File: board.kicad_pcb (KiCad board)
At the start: 2 copper layers, 49 parts, among them J1 TEMPS, J2 OLED, J3 Screw_Terminal_01x03, J4 Screw_Terminal_01x03, J5 PWR_IN, J6 CONN_PROG, J6 Conn_01x05_Female, K2 SRD-05VDC-SL-C, K3 SRD-05VDC-SL-C, Q1 BC847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

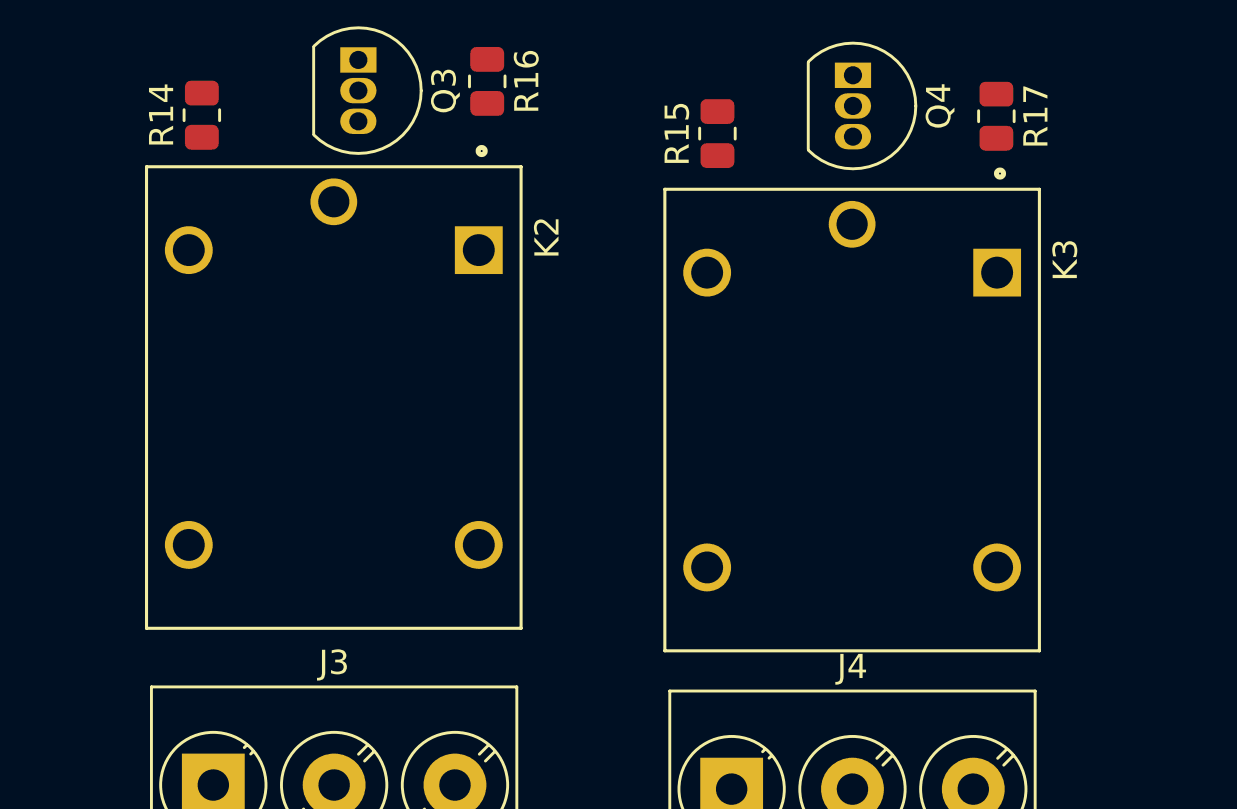
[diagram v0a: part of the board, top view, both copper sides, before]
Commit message: feat: added relative pathing for relay libs
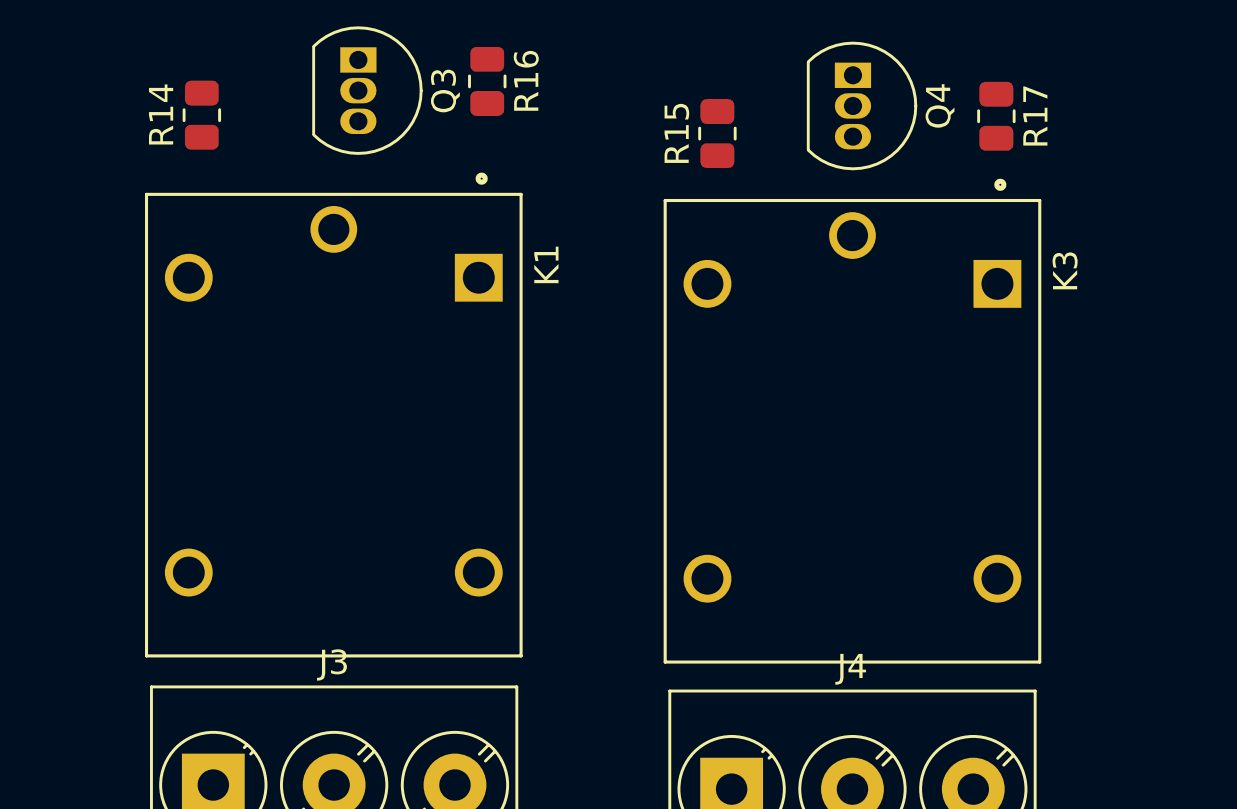
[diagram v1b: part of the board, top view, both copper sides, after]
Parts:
- removed K2: SRD-05VDC-SL-C, SRD-05VDC-SL-C:RELAY_SRD-05VDC-SL-C
- added K1: SRD-05VDC-SL-C, SRD-05VDC-SL-C:RELAY_SRD-05VDC-SL-C, F.Cu at (54.7, 97.4)
- moved K3 0.47 mm to (76.2, 97.7)
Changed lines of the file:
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@@
   (net 67 "Net-(J3-Pad1)")
   (net 68 "Net-(J3-Pad3)")
-  (net 69 "Net-(R17-Pad2)")
+  (net 69 "Net-(K3-PadA1)")
   (net 70 "Net-(J4-Pad2)")
   (net 71 "Net-(J4-Pad1)")
@@
       (net 64 "Net-(Q4-Pad1)") (pintype "passive"))
     (pad "2" smd roundrect (at 0.9125 0 270) (size 1.025 1.4) (layers "F.Cu" "F.Paste" "F.Mask") (roundrect_rratio 0.243902)
-      (net 69 "Net-(R17-Pad2)") (pintype "passive"))
+      (net 69 "Net-(K3-PadA1)") (pintype "passive"))
     (model "${KICAD6_3DMODEL_DIR}/Resistor_SMD.3dshapes/R_0805_2012Metric.wrl"
       (offset (xyz 0 0 0))
@@
     )
   )
+  (footprint "SRD-05VDC-SL-C:RELAY_SRD-05VDC-SL-C" (layer "F.Cu")
+    (at 54.737 97.409 -90)
+    (property "MANUFACTURER" "SONGLE RELAY")
+    (property "STANDARD" "IPC-7251")
+    (property "Sheetfile" "board.kicad_sch")
+    (property "Sheetname" "")
+    (attr through_hole)
+    (fp_text reference "K1" (at -6.62563 -8.83584 90) (layer "F.SilkS")
+      (effects (font (size 1.000094 1.000094) (thickness 0.15)))
+    )
+    (fp_text value "SRD-05VDC-SL-C" (at 2.90086 8.667695 90) (layer "F.Fab")
+      (effects (font (size 1.000307 1.000307) (thickness 0.15)))
+    )
+    (fp_line (start 9.55 7.75) (end -9.55 7.75) (layer "F.SilkS") (width 0.127))
+    (fp_line (start -9.55 7.75) (end -9.55 -7.75) (layer "F.SilkS") (width 0.127))
+    (fp_line (start -9.55 -7.75) (end 9.55 -7.75) (layer "F.SilkS") (width 0.127))
+    (fp_line (start 9.55 -7.75) (end 9.55 7.75) (layer "F.SilkS") (width 0.127))
+    (fp_circle (center -10.2 -6.119) (end -10.1 -6.119) (layer "F.SilkS") (width 0.3) (fill none))
+    (fp_line (start 9.8 -8) (end 9.8 8) (layer "F.CrtYd") (width 0.05))
+    (fp_line (start 9.8 8) (end -9.8 8) (layer "F.CrtYd") (width 0.05))
+    (fp_line (start -9.8 8) (end -9.8 -8) (layer "F.CrtYd") (width 0.05))
+    (fp_line (start -9.8 -8) (end 9.8 -8) (layer "F.CrtYd") (width 0.05))
+    (fp_line (start 9.55 -7.75) (end 9.55 7.75) (layer "F.Fab") (width 0.127))
+    (fp_line (start 9.55 7.75) (end -9.55 7.75) (layer "F.Fab") (width 0.127))
+    (fp_line (start -9.55 7.75) (end -9.55 -7.75) (layer "F.Fab") (width 0.127))
+    (fp_line (start -9.55 -7.75) (end 9.55 -7.75) (layer "F.Fab") (width 0.127))
+    (pad "A1" thru_hole rect (at -6.1 -6 270) (size 1.98 1.98) (drill 1.32) (layers *.Cu *.Mask)
+      (net 65 "Net-(R16-Pad2)") (pintype "passive"))
+    (pad "A2" thru_hole circle (at -6.1 6 270) (size 1.98 1.98) (drill 1.32) (layers *.Cu *.Mask)
+      (net 3 "VBUS") (pintype "passive"))
+    (pad "COM" thru_hole circle (at -8.1 0 270) (size 1.935 1.935) (drill 1.29) (layers *.Cu *.Mask)
+      (net 66 "Net-(J3-Pad2)") (pintype "passive"))
+    (pad "NC" thru_hole circle (at 6.1 -6 270) (size 1.98 1.98) (drill 1.32) (layers *.Cu *.Mask)
+      (net 68 "Net-(J3-Pad3)") (pintype "passive"))
+    (pad "NO" thru_hole circle (at 6.1 6 270) (size 1.98 1.98) (drill 1.32) (layers *.Cu *.Mask)
+      (net 67 "Net-(J3-Pad1)") (pintype "passive"))
+    (model "${KIPRJMOD}/libs/SRD-05VDC-SL-C/SRD-05VDC-SL-C.step"
+      (offset (xyz 9 7.5 0))
+      (scale (xyz 1 1 1))
+      (rotate (xyz 0 0 180))
+    )
+  )
   (footprint "Resistor_SMD:R_0805_2012Metric" (layer "F.Cu")
     (at 49.8035 52.514 180)
@@
   )
   (footprint "SRD-05VDC-SL-C:RELAY_SRD-05VDC-SL-C" (layer "F.Cu")
-    (at 54.737 96.266 -90)
+    (at 76.2 97.663 -90)
     (property "MANUFACTURER" "SONGLE RELAY")
     (property "STANDARD" "IPC-7251")
@@
     (property "Sheetname" "")
     (attr through_hole)
-    (fp_text reference "K2" (at -6.62563 -8.83584 90) (layer "F.SilkS")
+    (fp_text reference "K3" (at -6.62563 -8.83584 90) (layer "F.SilkS")
       (effects (font (size 1.000094 1.000094) (thickness 0.15)))
     )
@@
       (effects (font (size 1.000307 1.000307) (thickness 0.15)))
     )
-    (fp_line (start -9.55 -7.75) (end 9.55 -7.75) (layer "F.SilkS") (width 0.127))
     (fp_line (start 9.55 -7.75) (end 9.55 7.75) (layer "F.SilkS") (width 0.127))
     (fp_line (start -9.55 7.75) (end -9.55 -7.75) (layer "F.SilkS") (width 0.127))
+    (fp_line (start -9.55 -7.75) (end 9.55 -7.75) (layer "F.SilkS") (width 0.127))
     (fp_line (start 9.55 7.75) (end -9.55 7.75) (layer "F.SilkS") (width 0.127))
     (fp_circle (center -10.2 -6.119) (end -10.1 -6.119) (layer "F.SilkS") (width 0.3) (fill none))
+    (fp_line (start -9.8 -8) (end 9.8 -8) (layer "F.CrtYd") (width 0.05))
+    (fp_line (start 9.8 -8) (end 9.8 8) (layer "F.CrtYd") (width 0.05))
+    (fp_line (start 9.8 8) (end -9.8 8) (layer "F.CrtYd") (width 0.05))
     (fp_line (start -9.8 8) (end -9.8 -8) (layer "F.CrtYd") (width 0.05))
-    (fp_line (start 9.8 -8) (end 9.8 8) (layer "F.CrtYd") (width 0.05))
-    (fp_line (start -9.8 -8) (end 9.8 -8) (layer "F.CrtYd") (width 0.05))
-    (fp_line (start 9.8 8) (end -9.8 8) (layer "F.CrtYd") (width 0.05))
+    (fp_line (start 9.55 7.75) (end -9.55 7.75) (layer "F.Fab") (width 0.127))
+    (fp_line (start 9.55 -7.75) (end 9.55 7.75) (layer "F.Fab") (width 0.127))
     (fp_line (start -9.55 -7.75) (end 9.55 -7.75) (layer "F.Fab") (width 0.127))
-    (fp_line (start 9.55 -7.75) (end 9.55 7.75) (layer "F.Fab") (width 0.127))
-    (fp_line (start 9.55 7.75) (end -9.55 7.75) (layer "F.Fab") (width 0.127))
     (fp_line (start -9.55 7.75) (end -9.55 -7.75) (layer "F.Fab") (width 0.127))
-    (pad "A1" thru_hole rect locked (at -6.1 -6 270) (size 1.98 1.98) (drill 1.32) (layers *.Cu *.Mask)
-      (net 65 "Net-(R16-Pad2)") (pintype "passive"))
-    (pad "A2" thru_hole circle locked (at -6.1 6 270) (size 1.98 1.98) (drill 1.32) (layers *.Cu *.Mask)
+    (pad "A1" thru_hole rect (at -6.1 -6 270) (size 1.98 1.98) (drill 1.32) (layers *.Cu *.Mask)
+      (net 69 "Net-(K3-PadA1)") (pintype "passive"))
+    (pad "A2" thru_hole circle (at -6.1 6 270) (size 1.98 1.98) (drill 1.32) (layers *.Cu *.Mask)
       (net 3 "VBUS") (pintype "passive"))
-    (pad "COM" thru_hole circle locked (at -8.1 0 270) (size 1.935 1.935) (drill 1.29) (layers *.Cu *.Mask)
-      (net 66 "Net-(J3-Pad2)") (pintype "passive"))
-    (pad "NC" thru_hole circle locked (at 6.1 -6 270) (size 1.98 1.98) (drill 1.32) (layers *.Cu *.Mask)
-      (net 68 "Net-(J3-Pad3)") (pintype "passive"))
-    (pad "NO" thru_hole circle locked (at 6.1 6 270) (size 1.98 1.98) (drill 1.32) (layers *.Cu *.Mask)
-      (net 67 "Net-(J3-Pad1)") (pintype "passive"))
+    (pad "COM" thru_hole circle (at -8.1 0 270) (size 1.935 1.935) (drill 1.29) (layers *.Cu *.Mask)
+      (net 70 "Net-(J4-Pad2)") (pintype "passive"))
+    (pad "NC" thru_hole circle (at 6.1 -6 270) (size 1.98 1.98) (drill 1.32) (layers *.Cu *.Mask)
+      (net 72 "Net-(J4-Pad3)") (pintype "passive"))
+    (pad "NO" thru_hole circle (at 6.1 6 270) (size 1.98 1.98) (drill 1.32) (layers *.Cu *.Mask)
+      (net 71 "Net-(J4-Pad1)") (pintype "passive"))
+    (model "${KIPRJMOD}/libs/SRD-05VDC-SL-C/SRD-05VDC-SL-C.step"
+      (offset (xyz 9 7.5 0))
+      (scale (xyz 1 1 1))
+      (rotate (xyz 0 0 180))
+    )
   )
   (footprint "Resistor_SMD:R_0805_2012Metric" (layer "F.Cu")
@@
     )
   )
-  (footprint "SRD-05VDC-SL-C:RELAY_SRD-05VDC-SL-C" (layer "F.Cu")
-    (at 76.186 97.198 -90)
-    (property "MANUFACTURER" "SONGLE RELAY")
-    (property "STANDARD" "IPC-7251")
-    (property "Sheetfile" "board.kicad_sch")
-    (property "Sheetname" "")
-    (attr through_hole)
-    (fp_text reference "K3" (at -6.62563 -8.83584 90) (layer "F.SilkS")
-      (effects (font (size 1.000094 1.000094) (thickness 0.15)))
-    )
-    (fp_text value "SRD-05VDC-SL-C" (at 2.90086 8.667695 90) (layer "F.Fab")
-      (effects (font (size 1.000307 1.000307) (thickness 0.15)))
-    )
-    (fp_line (start 9.55 7.75) (end -9.55 7.75) (layer "F.SilkS") (width 0.127))
-    (fp_line (start -9.55 -7.75) (end 9.55 -7.75) (layer "F.SilkS") (width 0.127))
-    (fp_line (start 9.55 -7.75) (end 9.55 7.75) (layer "F.SilkS") (width 0.127))
-    (fp_line (start -9.55 7.75) (end -9.55 -7.75) (layer "F.SilkS") (width 0.127))
-    (fp_circle (center -10.2 -6.119) (end -10.1 -6.119) (layer "F.SilkS") (width 0.3) (fill none))
-    (fp_line (start -9.8 8) (end -9.8 -8) (layer "F.CrtYd") (width 0.05))
-    (fp_line (start -9.8 -8) (end 9.8 -8) (layer "F.CrtYd") (width 0.05))
-    (fp_line (start 9.8 -8) (end 9.8 8) (layer "F.CrtYd") (width 0.05))
-    (fp_line (start 9.8 8) (end -9.8 8) (layer "F.CrtYd") (width 0.05))
-    (fp_line (start 9.55 7.75) (end -9.55 7.75) (layer "F.Fab") (width 0.127))
-    (fp_line (start 9.55 -7.75) (end 9.55 7.75) (layer "F.Fab") (width 0.127))
-    (fp_line (start -9.55 7.75) (end -9.55 -7.75) (layer "F.Fab") (width 0.127))
-    (fp_line (start -9.55 -7.75) (end 9.55 -7.75) (layer "F.Fab") (width 0.127))
-    (pad "A1" thru_hole rect locked (at -6.1 -6 270) (size 1.98 1.98) (drill 1.32) (layers *.Cu *.Mask)
-      (net 69 "Net-(R17-Pad2)") (pintype "passive"))
-    (pad "A2" thru_hole circle locked (at -6.1 6 270) (size 1.98 1.98) (drill 1.32) (layers *.Cu *.Mask)
-      (net 3 "VBUS") (pintype "passive"))
-    (pad "COM" thru_hole circle locked (at -8.1 0 270) (size 1.935 1.935) (drill 1.29) (layers *.Cu *.Mask)
-      (net 70 "Net-(J4-Pad2)") (pintype "passive"))
-    (pad "NC" thru_hole circle locked (at 6.1 -6 270) (size 1.98 1.98) (drill 1.32) (layers *.Cu *.Mask)
-      (net 72 "Net-(J4-Pad3)") (pintype "passive"))
-    (pad "NO" thru_hole circle locked (at 6.1 6 270) (size 1.98 1.98) (drill 1.32) (layers *.Cu *.Mask)
-      (net 71 "Net-(J4-Pad1)") (pintype "passive"))
-  )
   (footprint "Button_Switch_THT:SW_PUSH_6mm_H13mm" (layer "F.Cu")

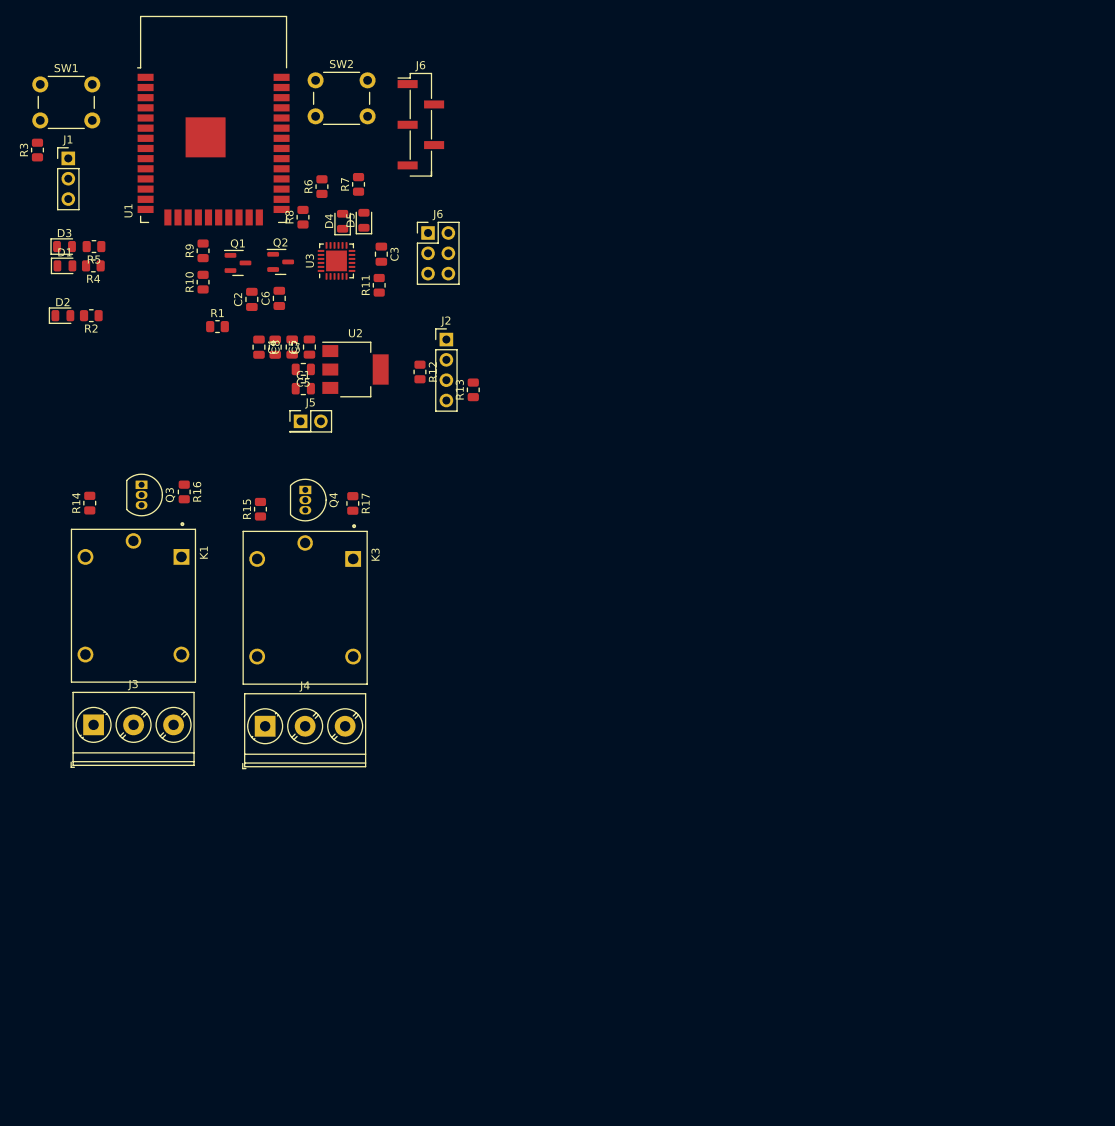
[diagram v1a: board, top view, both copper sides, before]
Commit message: feat: added usb-c connector and switched to ch340e
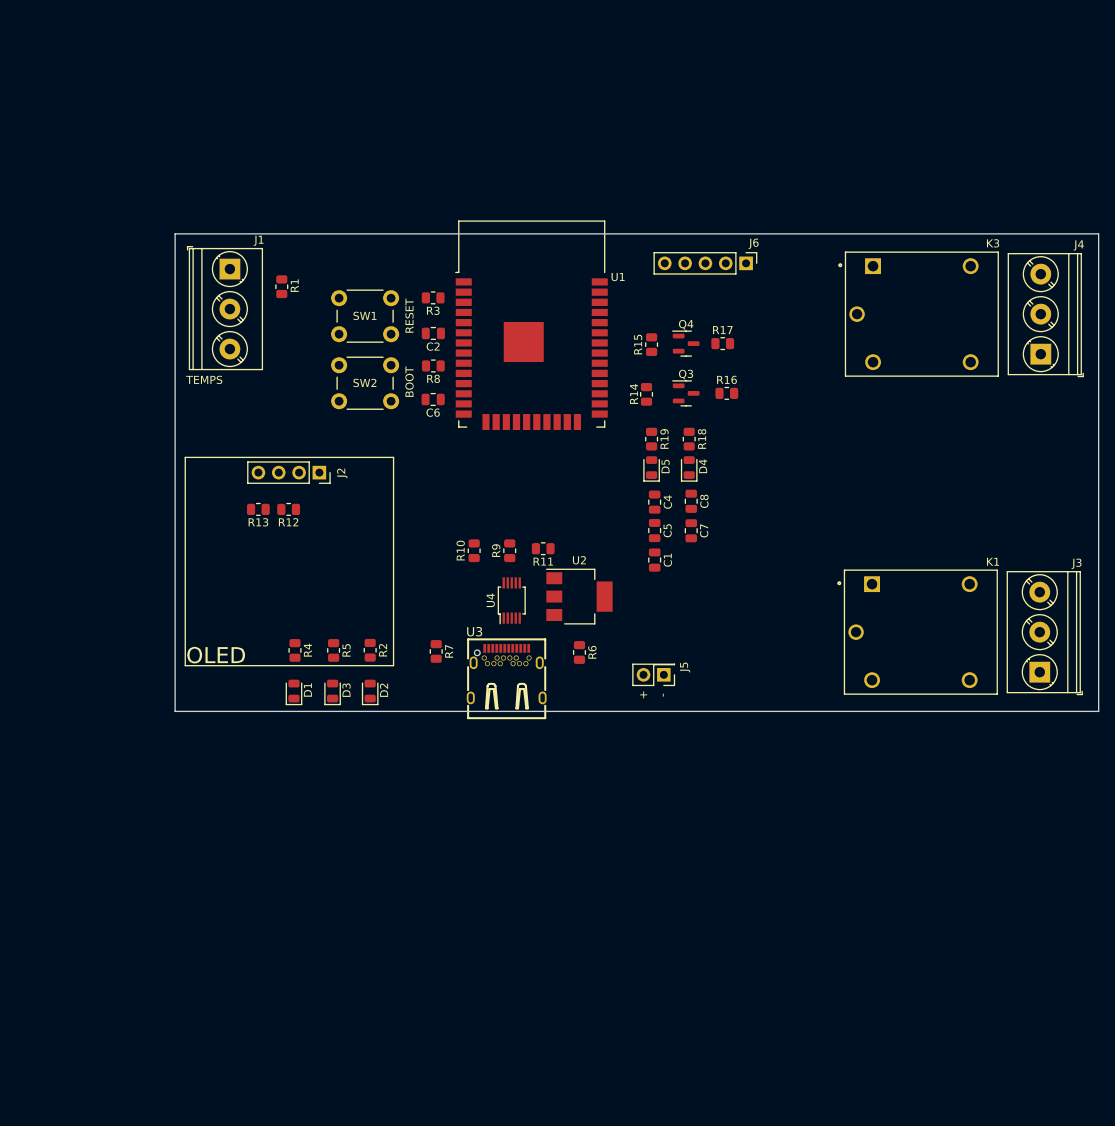
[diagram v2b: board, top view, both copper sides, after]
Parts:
- removed C3: 4.7uF, Capacitor_SMD:C_0805_2012Metric
- removed the C5 at (76.0, 67.9)
- removed the C5 at (74.6, 65.1)
- removed the J6 at (91.6, 50.8)
- removed the J6 at (90.7, 37.3)
- removed Q1, Q2: BC847, Package_TO_SOT_SMD:SOT-23
- added C5: 100nF, Capacitor_SMD:C_0805_2012Metric, F.Cu at (119.9, 88.0)
- added J6: PROG, Connector_PinHeader_2.54mm:PinHeader_1x05_P2.54mm_Vertical, F.Cu at (131.3, 54.6)
- added R18: 1k, Resistor_SMD:R_0805_2012Metric, F.Cu at (124.2, 76.6)
- added R19: 1k, Resistor_SMD:R_0805_2012Metric, F.Cu at (119.5, 76.6)
- added U4: CH340E, Package_SO:MSOP-10_3x3mm_P0.5mm, F.Cu at (102.0, 96.8)
- D4: value TXLED -> RXLED
- D5: value RXLED -> TXLED
- J1: footprint Connector_PinHeader_2.54mm:PinHeader_1x03_P2.54mm_Vertical -> TerminalBlock_Phoenix:TerminalBlock_Phoenix_PT-1,5-3-5.0-H_1x03_P5.00mm_Horizontal
- J2: footprint Connector_PinHeader_2.54mm:PinHeader_1x04_P2.54mm_Vertical -> Connector_PinSocket_2.54mm:PinSocket_1x04_P2.54mm_Vertical
- J3: value Screw_Terminal_01x03 -> HV1
- J4: value Screw_Terminal_01x03 -> HV2
- K1: value SRD-05VDC-SL-C -> RELAY1
- K3: value SRD-05VDC-SL-C -> RELAY2
- Q3, Q4: value BS170 -> AO3400A; footprint Package_TO_SOT_THT:TO-92_Inline -> Package_TO_SOT_SMD:SOT-23
- R10, R9: value 10k -> 0
- R11: value 4k7 -> 5k1
- R14, R15: value R -> 10k
- R16, R17: value R -> 0
- R6, R7: value 470 -> 5k1
- SW1: footprint Button_Switch_THT:SW_PUSH_6mm_H13mm -> Button_Switch_THT:SW_PUSH_6mm_H4.3mm
- SW2: value SW_RST -> SW_BOOT; footprint Button_Switch_THT:SW_PUSH_6mm_H13mm -> Button_Switch_THT:SW_PUSH_6mm_H4.3mm
- U1: value ESP32-WROOM-32(8MB) -> ESP32-WROOM-32
- U3: value CP2104 -> USB-306C; footprint Package_DFN_QFN:QFN-24-1EP_4x4mm_P0.5mm_EP2.6x2.6mm -> board:USB-TYPE-C-TH_USB-306C
- moved J3 118.5 mm to (168.0, 105.7), turned to 90 degrees
- moved J4 107.5 mm to (168.2, 66.0), turned to 90 degrees
- moved K1 98.5 mm to (153.2, 100.7), turned to 0 degrees
- moved K3 85.4 mm to (153.3, 61.0), turned to 0 degrees
- moved R14 70.9 mm to (118.9, 71.0)
- moved Q3 69.0 mm to (123.8, 70.9), turned to 0 degrees
- moved R16 68.9 mm to (128.9, 70.9), turned to 0 degrees
- moved R6 66.5 mm to (110.5, 103.3), turned to -90 degrees
- moved D3 64.9 mm to (79.6, 108.1), turned to 90 degrees
- moved D2 60.6 mm to (84.3, 108.1), turned to 90 degrees
- moved D1 60.4 mm to (74.8, 108.1), turned to 90 degrees
- moved R7 59.2 mm to (92.6, 103.1), turned to -90 degrees
- moved R5 58.7 mm to (79.8, 103.0), turned to -90 degrees
- moved U3 55.7 mm to (101.4, 105.8), turned to 0 degrees
- moved C8 55.5 mm to (124.5, 84.4)
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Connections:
- net RST renamed EN_ESP
- D4 pad 1: Net-(D4-Pad1) -> TX_CH
- D4 pad 2: +3V3 -> Net-(D4-Pad2)
- D5 pad 1: Net-(D5-Pad1) -> RX_CH
- D5 pad 2: +3V3 -> Net-(D5-Pad2)
- Q3 pad 1: Net-(Q3-Pad1) -> CH1
- Q3 pad 2: CH1 -> GND
- Q3 pad 3: GND -> Net-(Q3-Pad3)
- Q4 pad 1: Net-(Q4-Pad1) -> CH2
- Q4 pad 2: CH2 -> GND
- Q4 pad 3: GND -> Net-(Q4-Pad3)
- R10 pad 1: DTR -> RX_CH
- R10 pad 2: Net-(Q1-Pad1) -> TX_ESP
- R11 pad 1: +3V3 -> /NCTS
- R11 pad 2: Net-(R11-Pad2) -> GPIO0
- R16 pad 1: Net-(Q3-Pad1) -> Net-(Q3-Pad3)
- R17 pad 1: Net-(Q4-Pad1) -> Net-(Q4-Pad3)
- R6 pad 1: RX_ESP -> CC2
- R6 pad 2: Net-(R6-Pad2) -> GND
- R7 pad 1: Net-(R7-Pad1) -> CC1
- R7 pad 2: TX_ESP -> GND
- R9 pad 1: RTS -> TX_CH
- R9 pad 2: Net-(Q2-Pad1) -> RX_ESP
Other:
- board outline added: 115.4 x 59.7 mm
- board text added: "OLED"
